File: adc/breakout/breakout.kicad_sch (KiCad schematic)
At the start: 70 parts, among them J1 Conn_01x05_Pin, J2 Conn_01x06_Pin, J3 Conn_01x05_Pin, J4 Conn_01x03_Pin, U1 ESD5344D-TP, U2 ESD5344D-TP, U3 ADS1261B, U4 ESD5344D-TP, U5 TPS7A2050PDBVR, U6 TPS61252DSG, U7 XC6206P332MR

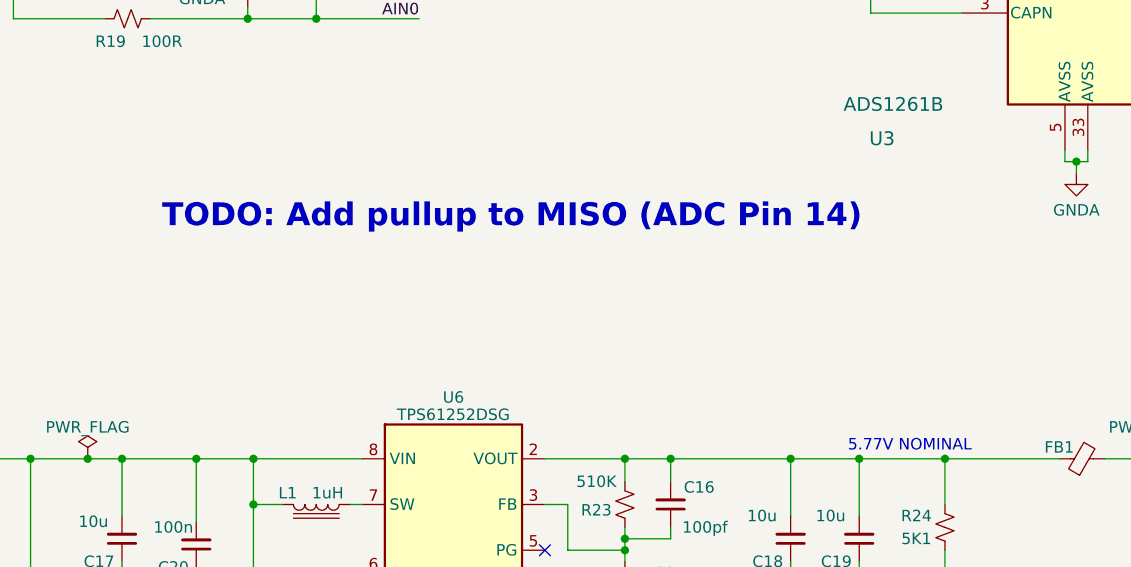
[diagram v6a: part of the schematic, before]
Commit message: Added comment to the ADC breakout schematic.
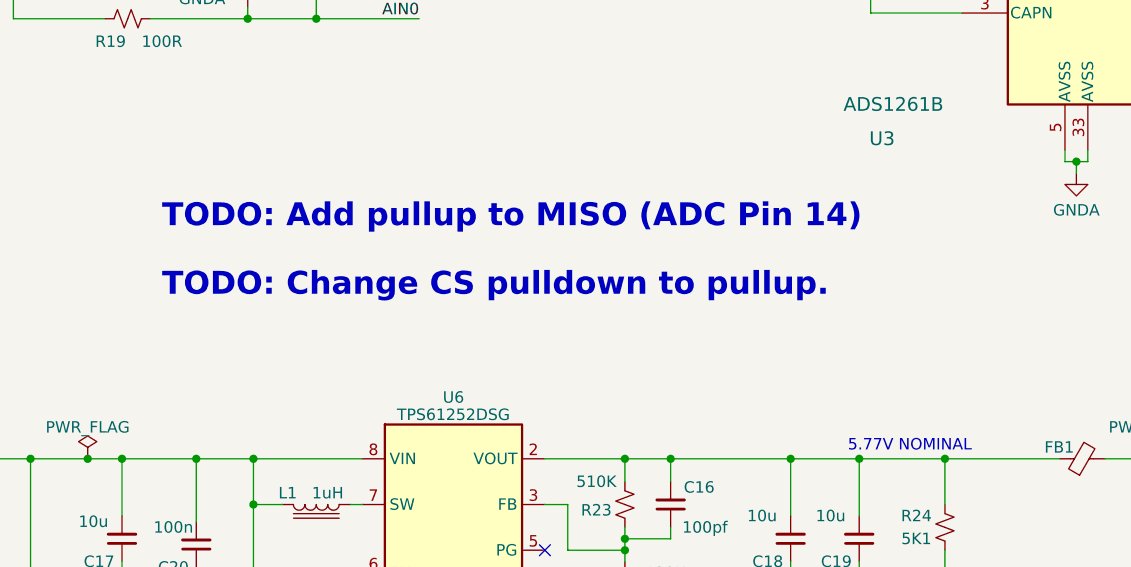
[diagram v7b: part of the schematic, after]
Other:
- note added: "TODO: Change CS pulldown to pullup."
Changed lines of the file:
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@@
     (effects (font (size 1.27 1.27)) (justify left bottom))
+  )
+  (text "TODO: Change CS pulldown to pullup." (at 74.295 125.73 0)
+    (effects (font (size 2.54 2.54) (thickness 0.508) bold (color 255 0 0 1)) (justify left bottom))
   )
   (text "5V" (at 35.56 145.415 0)

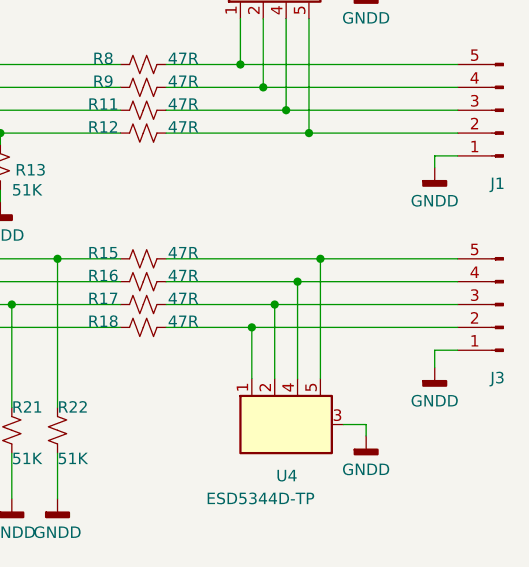
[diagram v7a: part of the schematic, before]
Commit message: Added net names to ADC breakout board schematic.
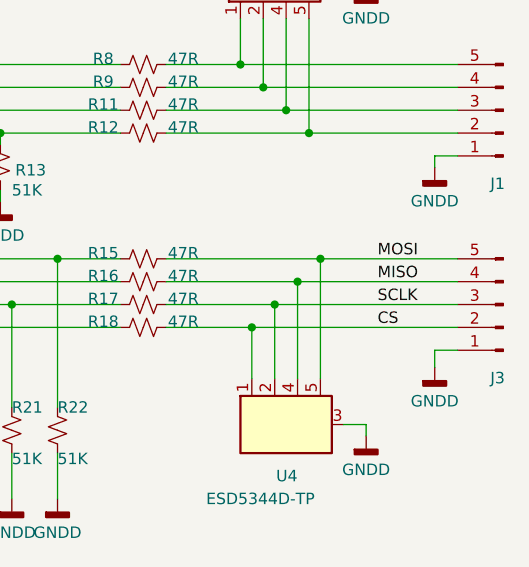
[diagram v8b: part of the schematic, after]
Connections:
- net CS: now reaches J3.2 (Pin_2), R18.1, U4.1 (D1)
- net SCLK: now reaches J3.3 (Pin_3), R17.1, U4.2 (D2)
- net MISO: now reaches J3.4 (Pin_4), R16.1, U4.4 (D3)
- net MOSI: now reaches J3.5 (Pin_5), R15.1, U4.5 (D4)
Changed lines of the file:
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@@
     (effects (font (size 1.27 1.27)) (justify right bottom))
+  )
+  (label "MOSI" (at 260.985 85.09 0) (fields_autoplaced)
+    (effects (font (size 1.27 1.27)) (justify left bottom))
   )
   (label "AIN3" (at 139.7 74.93 0) (fields_autoplaced)
     (effects (font (size 1.27 1.27)) (justify left bottom))
   )
+  (label "CS" (at 260.985 92.71 0) (fields_autoplaced)
+    (effects (font (size 1.27 1.27)) (justify left bottom))
+  )
   (label "AIN2" (at 139.7 77.47 0) (fields_autoplaced)
+    (effects (font (size 1.27 1.27)) (justify left bottom))
+  )
+  (label "SCLK" (at 260.985 90.17 0) (fields_autoplaced)
     (effects (font (size 1.27 1.27)) (justify left bottom))
   )
@@
     (effects (font (size 1.27 1.27)) (justify right bottom))
   )
+  (label "MISO" (at 260.985 87.63 0) (fields_autoplaced)
+    (effects (font (size 1.27 1.27)) (justify left bottom))
+  )
   (label "AIN1" (at 102.87 79.375 180) (fields_autoplaced)
